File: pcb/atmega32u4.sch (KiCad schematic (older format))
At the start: 15 parts, among them CON1 ISP, P1 CONN_01X14, P2 CONN_01X14, P3 USB_OTG, U1 ATmega32U4-AU, Y1 16MHz

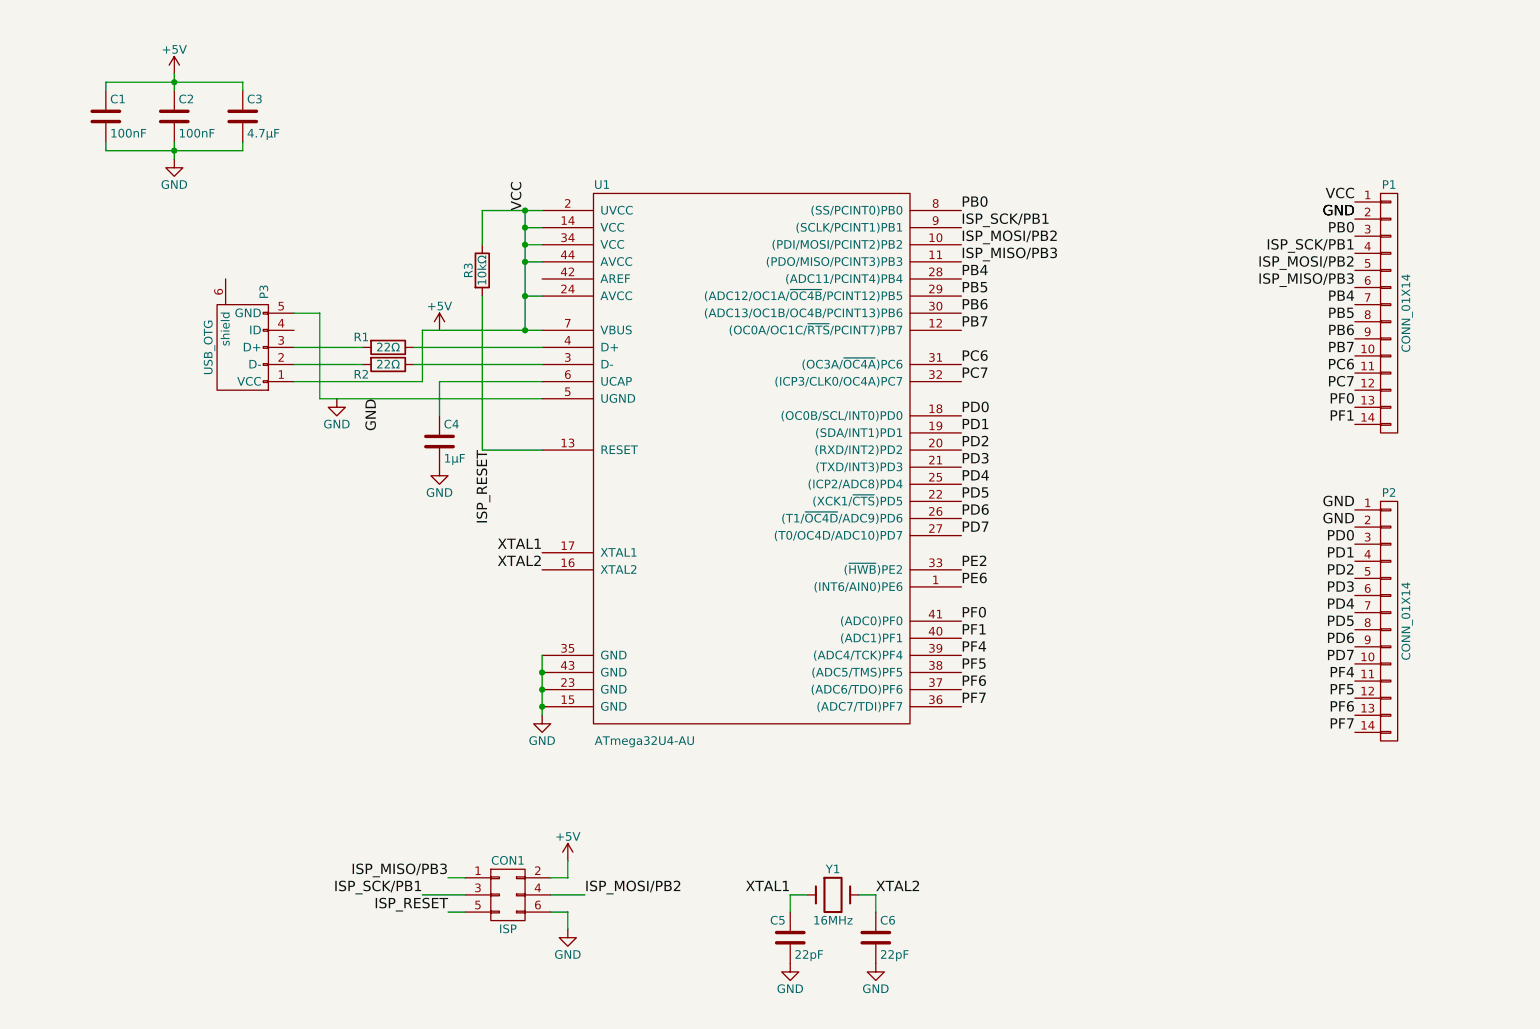
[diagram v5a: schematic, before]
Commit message: Fix up schematic accoring to adafruit
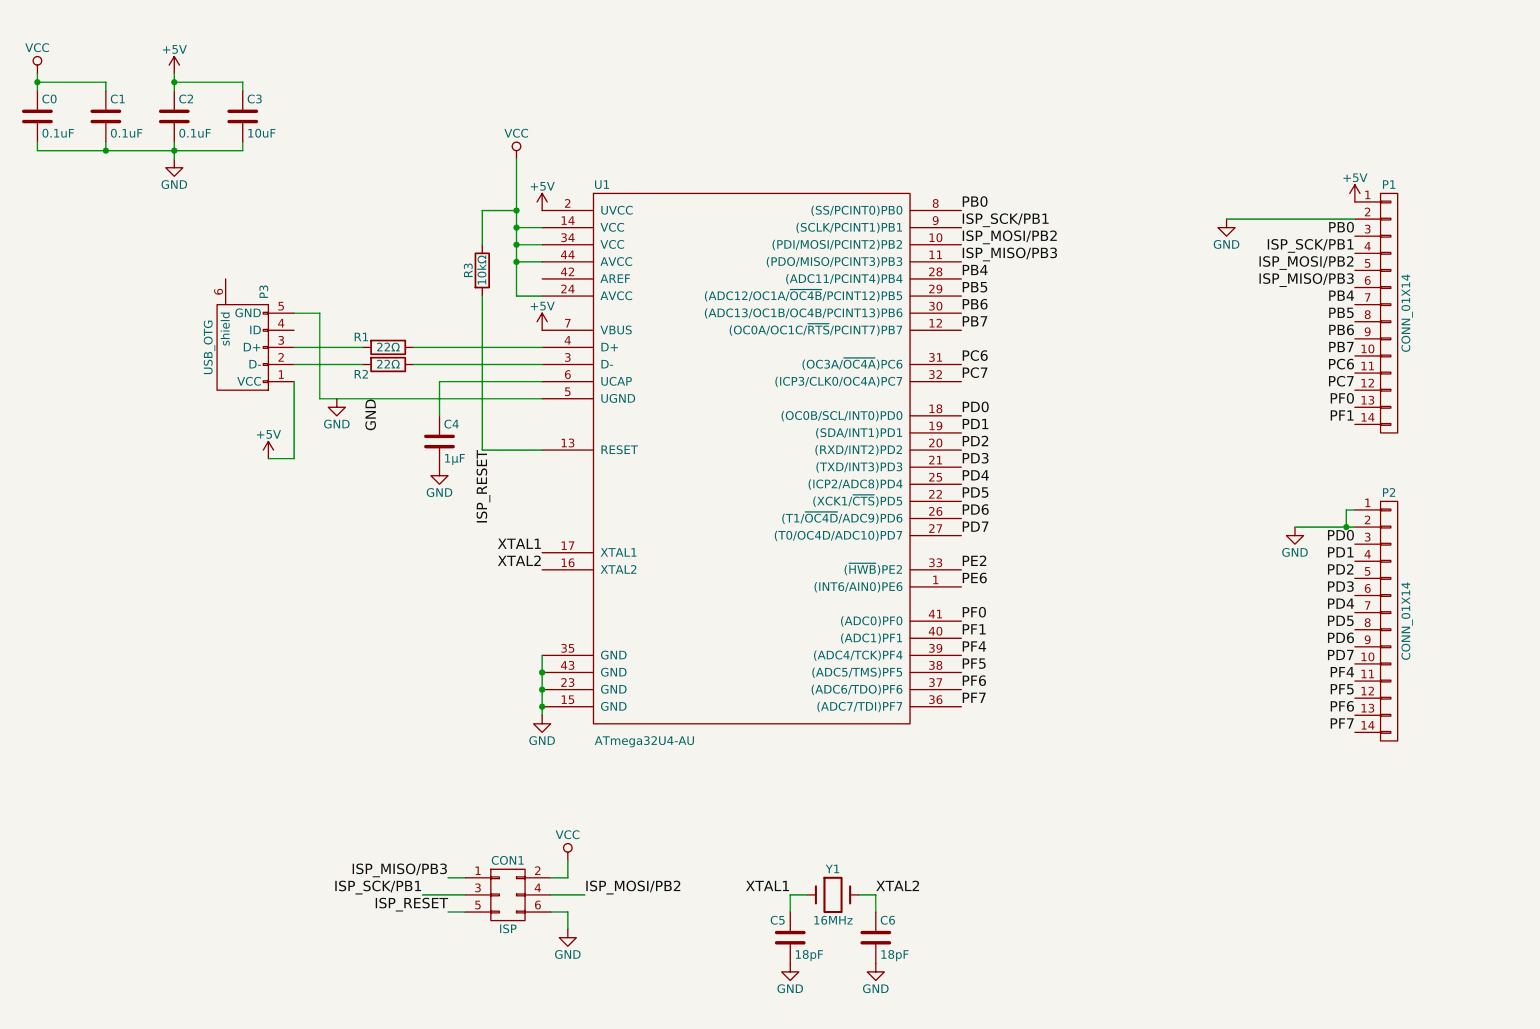
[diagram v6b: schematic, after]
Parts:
- added C0: 0.1uF, Capacitors_SMD:C_0805_HandSoldering, symbol C
- C1, C2: value 100nF -> 0.1uF
- C3: value 4.7µF -> 10uF
- C5, C6: value 22pF -> 18pF
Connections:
- net +5V: now also P1.1 (P1), P3.1 (VCC), U1.2 (UVCC), U1.7 (VBUS); no longer C1.1, CON1.2 (P2)
- net GND: now also C0.2
- net VCC: now also C1.1, CON1.2 (P2), C0.1; no longer P1.1 (P1), P3.1 (VCC), U1.2 (UVCC), U1.7 (VBUS)
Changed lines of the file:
@@
 P 1300 1350
 F 0 "C1" H 1325 1450 50  0000 L CNN
-F 1 "100nF" H 1325 1250 50  0000 L CNN
+F 1 "0.1uF" H 1325 1250 50  0000 L CNN
 F 2 "Capacitors_SMD:C_0805_HandSoldering" H 1338 1200 50  0001 C CNN
 F 3 "" H 1300 1350 50  0000 C CNN
@@
 P 1700 1350
 F 0 "C2" H 1725 1450 50  0000 L CNN
-F 1 "100nF" H 1725 1250 50  0000 L CNN
+F 1 "0.1uF" H 1725 1250 50  0000 L CNN
 F 2 "Capacitors_SMD:C_0805_HandSoldering" H 1738 1200 50  0001 C CNN
 F 3 "" H 1700 1350 50  0000 C CNN
@@
 P 2100 1350
 F 0 "C3" H 2125 1450 50  0000 L CNN
-F 1 "4.7µF" H 2125 1250 50  0000 L CNN
+F 1 "10uF" H 2125 1250 50  0000 L CNN
 F 2 "Capacitors_SMD:C_0805_HandSoldering" H 2138 1200 50  0001 C CNN
 F 3 "" H 2100 1350 50  0000 C CNN
@@
 	1    0    0    -1
 $EndComp
-Connection ~ 3750 2400
-Wire Wire Line
-	3500 1900 3850 1900
-Wire Wire Line
-	3500 3300 3500 2400
-Wire Wire Line
-	3850 3300 3500 3300
-Connection ~ 1700 1550
-Wire Wire Line
-	2100 1550 2100 1500
-Wire Wire Line
-	1300 1550 1300 1500
-Wire Wire Line
-	1300 1550 2100 1550
-Wire Wire Line
-	1700 1500 1700 1600
-Wire Wire Line
-	2100 1150 2100 1200
-Connection ~ 1700 1150
-Wire Wire Line
-	1300 1150 1300 1200
-Wire Wire Line
-	1300 1150 2100 1150
-Wire Wire Line
-	1700 1100 1700 1200
-Wire Wire Line
-	3850 4500 3850 4850
-Connection ~ 3850 4600
-Connection ~ 3850 4700
-Connection ~ 3850 4800
-Wire Wire Line
-	3850 2700 3100 2700
-Wire Wire Line
-	3100 2800 3850 2800
-Wire Wire Line
-	2800 2700 2400 2700
-Wire Wire Line
-	2400 2800 2800 2800
-Wire Wire Line
-	3150 2600 3850 2600
-Wire Wire Line
-	3150 2600 3150 2900
-Wire Wire Line
-	3150 2900 2400 2900
-Wire Wire Line
-	3750 2400 3850 2400
-Wire Wire Line
-	3750 1900 3750 2600
-Connection ~ 3750 2600
-Wire Wire Line
-	3850 3000 2550 3000
-Wire Wire Line
-	2550 3000 2550 2500
-Wire Wire Line
-	2550 2500 2400 2500
-Wire Wire Line
-	3850 2900 3250 2900
-Wire Wire Line
-	3250 2900 3250 3100
-Wire Wire Line
-	3500 1900 3500 2100
-Connection ~ 3750 1900
-Wire Wire Line
-	3850 2100 3750 2100
-Connection ~ 3750 2100
-Wire Wire Line
-	3750 2000 3850 2000
-Connection ~ 3750 2000
-Wire Wire Line
-	3850 2200 3750 2200
-Connection ~ 3750 2200
 Text Label 3550 3300 3    60   ~ 0
 ISP_RESET
@@
 Text Label 6300 2000 0    60   ~ 0
 ISP_SCK/PB1
-Wire Wire Line
-	3900 5800 4000 5800
-Wire Wire Line
-	4000 5800 4000 5700
-$Comp
-L +5V #PWR06
-U 1 1 57DFE2FD
-P 4000 5700
-F 0 "#PWR06" H 4000 5550 50  0001 C CNN
-F 1 "+5V" H 4000 5840 50  0000 C CNN
-F 2 "" H 4000 5700 50  0000 C CNN
-F 3 "" H 4000 5700 50  0000 C CNN
-	1    4000 5700
-	1    0    0    -1
-$EndComp
-Wire Wire Line
-	3900 6000 4000 6000
-Wire Wire Line
-	4000 6000 4000 6100
 $Comp
 L GND #PWR07
@@
 	1    0    0    -1
 $EndComp
-Wire Wire Line
-	3900 5900 4100 5900
 Text Label 4100 5900 0    60   ~ 0
 ISP_MOSI/PB2
-Wire Wire Line
-	3400 5900 3150 5900
 Text Label 3300 5800 2    60   ~ 0
 ISP_MISO/PB3
-Wire Wire Line
-	3400 5800 3300 5800
 Text Label 3150 5900 2    60   ~ 0
 ISP_SCK/PB1
-Wire Wire Line
-	3400 6000 3300 6000
 Text Label 3300 6000 2    60   ~ 0
 ISP_RESET
@@
 	1    0    0    -1
 $EndComp
-Wire Wire Line
-	5700 5900 5800 5900
-Wire Wire Line
-	5800 5900 5800 6000
-Wire Wire Line
-	5400 5900 5300 5900
-Wire Wire Line
-	5300 5900 5300 6000
 $Comp
 L C C6
@@
 P 5800 6150
 F 0 "C6" H 5825 6250 50  0000 L CNN
-F 1 "22pF" H 5825 6050 50  0000 L CNN
+F 1 "18pF" H 5825 6050 50  0000 L CNN
 F 2 "Capacitors_SMD:C_0805_HandSoldering" H 5838 6000 50  0001 C CNN
 F 3 "" H 5800 6150 50  0000 C CNN
@@
 P 5300 6150
 F 0 "C5" H 5182 6250 50  0000 L CNN
-F 1 "22pF" H 5325 6050 50  0000 L CNN
+F 1 "18pF" H 5325 6050 50  0000 L CNN
 F 2 "Capacitors_SMD:C_0805_HandSoldering" H 5338 6000 50  0001 C CNN
 F 3 "" H 5300 6150 50  0000 C CNN
@@
 	1    0    0    -1
 $EndComp
-Text Label 3750 1900 1    60   ~ 0
-VCC
 Text Label 2900 3000 3    60   ~ 0
-GND
-Text Label 8600 1850 2    60   ~ 0
-VCC
-Text Label 8600 1950 2    60   ~ 0
 GND
 Text Label 6300 1900 0    60   ~ 0
@@
 Text Label 8600 2950 2    60   ~ 0
 PC7
-Text Label 8600 1950 2    60   ~ 0
-GND
-Text Label 8600 3650 2    60   ~ 0
-GND
-Text Label 8600 3750 2    60   ~ 0
-GND
 Text Label 8600 3850 2    60   ~ 0
 PD0
@@
 L +5V #PWR010
 U 1 1 57E26C1F
-P 3250 2600
-F 0 "#PWR010" H 3250 2450 50  0001 C CNN
-F 1 "+5V" H 3250 2740 50  0000 C CNN
-F 2 "" H 3250 2600 50  0000 C CNN
-F 3 "" H 3250 2600 50  0000 C CNN
-	1    3250 2600
-	1    0    0    -1
-$EndComp
+P 3850 2600
+F 0 "#PWR010" H 3850 2450 50  0001 C CNN
+F 1 "+5V" H 3850 2740 50  0000 C CNN
+F 2 "" H 3850 2600 50  0000 C CNN
+F 3 "" H 3850 2600 50  0000 C CNN
+	1    3850 2600
+	1    0    0    -1
+$EndComp
+$Comp
+L +5V #PWR?
+U 1 1 57EB4CAF
+P 2250 3350
+F 0 "#PWR?" H 2250 3200 50  0001 C CNN
+F 1 "+5V" H 2250 3490 50  0000 C CNN
+F 2 "" H 2250 3350 50  0000 C CNN
+F 3 "" H 2250 3350 50  0000 C CNN
+	1    2250 3350
+	1    0    0    -1
+$EndComp
+$Comp
+L +5V #PWR?
+U 1 1 57EB53DC
+P 3850 1900
+F 0 "#PWR?" H 3850 1750 50  0001 C CNN
+F 1 "+5V" H 3850 2040 50  0000 C CNN
+F 2 "" H 3850 1900 50  0000 C CNN
+F 3 "" H 3850 1900 50  0000 C CNN
+	1    3850 1900
+	1    0    0    -1
+$EndComp
+$Comp
+L VCC #PWR?
+U 1 1 57EB59BD
+P 4000 5700
+F 0 "#PWR?" H 4000 5550 50  0001 C CNN
+F 1 "VCC" H 4000 5850 50  0000 C CNN
+F 2 "" H 4000 5700 50  0000 C CNN
+F 3 "" H 4000 5700 50  0000 C CNN
+	1    4000 5700
+	1    0    0    -1
+$EndComp
+$Comp
+L VCC #PWR?
+U 1 1 57EB5AB2
+P 3700 1600
+F 0 "#PWR?" H 3700 1450 50  0001 C CNN
+F 1 "VCC" H 3700 1750 50  0000 C CNN
+F 2 "" H 3700 1600 50  0000 C CNN
+F 3 "" H 3700 1600 50  0000 C CNN
+	1    3700 1600
+	1    0    0    -1
+$EndComp
+$Comp
+L +5V #PWR?
+U 1 1 57EB5C21
+P 8600 1850
+F 0 "#PWR?" H 8600 1700 50  0001 C CNN
+F 1 "+5V" H 8600 1990 50  0000 C CNN
+F 2 "" H 8600 1850 50  0000 C CNN
+F 3 "" H 8600 1850 50  0000 C CNN
+	1    8600 1850
+	1    0    0    -1
+$EndComp
+$Comp
+L GND #PWR?
+U 1 1 57EB5F9C
+P 8250 3750
+F 0 "#PWR?" H 8250 3500 50  0001 C CNN
+F 1 "GND" H 8250 3600 50  0000 C CNN
+F 2 "" H 8250 3750 50  0000 C CNN
+F 3 "" H 8250 3750 50  0000 C CNN
+	1    8250 3750
+	1    0    0    -1
+$EndComp
+Wire Wire Line
+	3500 3300 3500 2400
+Wire Wire Line
+	3850 3300 3500 3300
+Connection ~ 1700 1550
+Wire Wire Line
+	2100 1550 2100 1500
+Wire Wire Line
+	1300 1550 1300 1500
+Wire Wire Line
+	900  1550 2100 1550
+Wire Wire Line
+	1700 1500 1700 1600
+Wire Wire Line
+	3850 4500 3850 4850
+Connection ~ 3850 4600
+Connection ~ 3850 4700
+Connection ~ 3850 4800
+Wire Wire Line
+	3850 2700 3100 2700
+Wire Wire Line
+	3100 2800 3850 2800
+Wire Wire Line
+	2800 2700 2400 2700
+Wire Wire Line
+	2400 2800 2800 2800
+Wire Wire Line
+	3850 3000 2550 3000
+Wire Wire Line
+	2550 3000 2550 2500
+Wire Wire Line
+	2550 2500 2400 2500
+Wire Wire Line
+	3850 2900 3250 2900
+Wire Wire Line
+	3250 2900 3250 3100
+Wire Wire Line
+	3900 5800 4000 5800
+Wire Wire Line
+	4000 5800 4000 5700
+Wire Wire Line
+	3900 6000 4000 6000
+Wire Wire Line
+	4000 6000 4000 6100
+Wire Wire Line
+	3900 5900 4100 5900
+Wire Wire Line
+	3400 5900 3150 5900
+Wire Wire Line
+	3400 5800 3300 5800
+Wire Wire Line
+	3400 6000 3300 6000
+Wire Wire Line
+	5700 5900 5800 5900
+Wire Wire Line
+	5800 5900 5800 6000
+Wire Wire Line
+	5400 5900 5300 5900
+Wire Wire Line
+	5300 5900 5300 6000
+Wire Wire Line
+	2400 2900 2400 3350
+Wire Wire Line
+	2400 3350 2250 3350
+Wire Wire Line
+	3850 2400 3700 2400
+Wire Wire Line
+	3700 2400 3700 1600
+Wire Wire Line
+	3850 2200 3700 2200
+Connection ~ 3700 2200
+Wire Wire Line
+	3850 2100 3700 2100
+Connection ~ 3700 2100
+Wire Wire Line
+	3850 2000 3700 2000
+Connection ~ 3700 2000
+Wire Wire Line
+	8250 3750 8600 3750
+Wire Wire Line
+	8600 3650 8550 3650
+Wire Wire Line
+	8550 3650 8550 3750
+Connection ~ 8550 3750
+Wire Wire Line
+	7850 1950 8600 1950
+$Comp
+L GND #PWR?
+U 1 1 57EB672F
+P 7850 1950
+F 0 "#PWR?" H 7850 1700 50  0001 C CNN
+F 1 "GND" H 7850 1800 50  0000 C CNN
+F 2 "" H 7850 1950 50  0000 C CNN
+F 3 "" H 7850 1950 50  0000 C CNN
+	1    7850 1950
+	1    0    0    -1
+$EndComp
+$Comp
+L C C0
+U 1 1 57EBA764
+P 900 1350
+F 0 "C0" H 925 1450 50  0000 L CNN
+F 1 "0.1uF" H 925 1250 50  0000 L CNN
+F 2 "Capacitors_SMD:C_0805_HandSoldering" H 938 1200 50  0001 C CNN
+F 3 "" H 900 1350 50  0000 C CNN
+	1    900  1350
+	1    0    0    -1
+$EndComp
+$Comp
+L VCC #PWR?
+U 1 1 57EBA95D
+P 900 1100
+F 0 "#PWR?" H 900 950 50  0001 C CNN
+F 1 "VCC" H 900 1250 50  0000 C CNN
+F 2 "" H 900 1100 50  0000 C CNN
+F 3 "" H 900 1100 50  0000 C CNN
+	1    900  1100
+	1    0    0    -1
+$EndComp
+Wire Wire Line
+	900  1100 900  1200
+Wire Wire Line
+	900  1150 1300 1150
+Wire Wire Line
+	1300 1150 1300 1200
+Connection ~ 900  1150
+Wire Wire Line
+	1700 1100 1700 1200
+Wire Wire Line
+	1700 1150 2100 1150
+Wire Wire Line
+	2100 1150 2100 1200
+Connection ~ 1700 1150
+Wire Wire Line
+	900  1500 900  1550
+Connection ~ 1300 1550
+Wire Wire Line
+	3500 2100 3500 1900
+Wire Wire Line
+	3500 1900 3700 1900
+Connection ~ 3700 1900
 $EndSCHEMATC

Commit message: Rearrange pins
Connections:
- net GND: no longer P2.2 (P2)
- net ISP_MISO/PB3: now also P2.10 (P10); no longer P1.6 (P6)
- net ISP_MOSI/PB2: now also P2.11 (P11); no longer P1.5 (P5)
- net ISP_SCK/PB1: now also P2.12 (P12); no longer P1.4 (P4)
- net PB0: now also P2.13 (P13); no longer P1.3 (P3)
- net PB4: now also P1.14 (P14); no longer P1.7 (P7)
- net PB5: now also P1.13 (P13); no longer P1.8 (P8)
- net PB6: now also P1.12 (P12); no longer P1.9 (P9)
- net PB7: now also P1.11 (P11); no longer P1.10 (P10)
- net PC6: now also P1.10 (P10); no longer P1.11 (P11)
- net PC7: now also P1.9 (P9); no longer P1.12 (P12)
- net PD0: now also P2.9 (P9); no longer P2.3 (P3)
- net PD1: now also P2.8 (P8); no longer P2.4 (P4)
- net PD2: now also P2.7 (P7); no longer P2.5 (P5)
- net PD4: now also P2.5 (P5); no longer P2.7 (P7)
- net PD5: now also P2.4 (P4); no longer P2.8 (P8)
- net PD6: now also P2.3 (P3); no longer P2.9 (P9)
- net PD7: now also P2.2 (P2); no longer P2.10 (P10)
- net PF0: now also P1.3 (P3); no longer P1.13 (P13)
- net PF1: now also P1.4 (P4); no longer P1.14 (P14)
- net PF4: now also P1.5 (P5); no longer P2.11 (P11)
- net PF5: now also P1.6 (P6); no longer P2.12 (P12)
- net PF6: now also P1.7 (P7); no longer P2.13 (P13)
- net PF7: now also P1.8 (P8); no longer P2.14 (P14)
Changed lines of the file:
@@
 Text Label 6300 4800 0    60   ~ 0
 PF7
-Text Label 8600 2250 2    60   ~ 0
+Text Label 8600 4650 2    60   ~ 0
 ISP_MOSI/PB2
-Text Label 8600 2350 2    60   ~ 0
+Text Label 8600 4550 2    60   ~ 0
 ISP_MISO/PB3
-Text Label 8600 2150 2    60   ~ 0
+Text Label 8600 4750 2    60   ~ 0
 ISP_SCK/PB1
-Text Label 8600 2050 2    60   ~ 0
+Text Label 8600 4850 2    60   ~ 0
 PB0
-Text Label 8600 2450 2    60   ~ 0
+Text Label 8600 3150 2    60   ~ 0
 PB4
-Text Label 8600 2550 2    60   ~ 0
+Text Label 8600 3050 2    60   ~ 0
 PB5
+Text Label 8600 2950 2    60   ~ 0
+PB6
+Text Label 8600 2850 2    60   ~ 0
+PB7
+Text Label 8600 2750 2    60   ~ 0
+PC6
 Text Label 8600 2650 2    60   ~ 0
-PB6
-Text Label 8600 2750 2    60   ~ 0
-PB7
-Text Label 8600 2850 2    60   ~ 0
-PC6
-Text Label 8600 2950 2    60   ~ 0
 PC7
-Text Label 8600 3850 2    60   ~ 0
+Text Label 8600 4450 2    60   ~ 0
 PD0
-Text Label 8600 3950 2    60   ~ 0
+Text Label 8600 4350 2    60   ~ 0
 PD1
-Text Label 8600 4050 2    60   ~ 0
+Text Label 8600 4250 2    60   ~ 0
 PD2
 Text Label 8600 4150 2    60   ~ 0
 PD3
-Text Label 8600 4250 2    60   ~ 0
+Text Label 8600 4050 2    60   ~ 0
 PD4
-Text Label 8600 4350 2    60   ~ 0
+Text Label 8600 3950 2    60   ~ 0
 PD5
-Text Label 8600 4450 2    60   ~ 0
+Text Label 8600 3850 2    60   ~ 0
 PD6
-Text Label 8600 4550 2    60   ~ 0
+Text Label 8600 3750 2    60   ~ 0
 PD7
 $Comp
@@
 	1    0    0    -1
 $EndComp
-Text Label 8600 3050 2    60   ~ 0
+Text Label 8600 2050 2    60   ~ 0
 PF0
-Text Label 8600 3150 2    60   ~ 0
+Text Label 8600 2150 2    60   ~ 0
 PF1
-Text Label 8600 4650 2    60   ~ 0
+Text Label 8600 2250 2    60   ~ 0
 PF4
-Text Label 8600 4750 2    60   ~ 0
+Text Label 8600 2350 2    60   ~ 0
 PF5
-Text Label 8600 4850 2    60   ~ 0
+Text Label 8600 2450 2    60   ~ 0
 PF6
-Text Label 8600 4950 2    60   ~ 0
+Text Label 8600 2550 2    60   ~ 0
 PF7
 $Comp
@@
 L GND #PWR?
 U 1 1 57EB5F9C
-P 8250 3750
-F 0 "#PWR?" H 8250 3500 50  0001 C CNN
-F 1 "GND" H 8250 3600 50  0000 C CNN
-F 2 "" H 8250 3750 50  0000 C CNN
-F 3 "" H 8250 3750 50  0000 C CNN
-	1    8250 3750
+P 8250 3650
+F 0 "#PWR?" H 8250 3400 50  0001 C CNN
+F 1 "GND" H 8250 3500 50  0000 C CNN
+F 2 "" H 8250 3650 50  0000 C CNN
+F 3 "" H 8250 3650 50  0000 C CNN
+	1    8250 3650
 	1    0    0    -1
 $EndComp
@@
 	3850 2000 3700 2000
 Connection ~ 3700 2000
-Wire Wire Line
-	8250 3750 8600 3750
-Wire Wire Line
-	8600 3650 8550 3650
-Wire Wire Line
-	8550 3650 8550 3750
-Connection ~ 8550 3750
 Wire Wire Line
 	7850 1950 8600 1950
@@
 	3500 1900 3700 1900
 Connection ~ 3700 1900
+Wire Wire Line
+	8600 3650 8250 3650
 $EndSCHEMATC

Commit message: Add LEDs
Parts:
- added D1: RED, symbol LED
- added D2: GREED, symbol LED
- added R4, R5: 1K, symbol R
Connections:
- net +5V: now also R5.1
- net GND: now also D1.1 (K), D2.1 (K)
- net PE6: now also P2.14 (P14), R4.1
- new net: D1.2 (A), R4.2
- new net: D2.2 (A), R5.2
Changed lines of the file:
@@
 Wire Wire Line
 	8600 3650 8250 3650
+$Comp
+L R R4
+U 1 1 57EBBD06
+P 8600 5100
+F 0 "R4" V 8680 5100 50  0000 C CNN
+F 1 "1K" V 8600 5100 50  0000 C CNN
+F 2 "" V 8530 5100 50  0000 C CNN
+F 3 "" H 8600 5100 50  0000 C CNN
+	1    8600 5100
+	1    0    0    -1
+$EndComp
+$Comp
+L LED D1
+U 1 1 57EBBDD1
+P 8600 5450
+F 0 "D1" H 8600 5550 50  0000 C CNN
+F 1 "RED" H 8600 5350 50  0000 C CNN
+F 2 "" H 8600 5450 50  0000 C CNN
+F 3 "" H 8600 5450 50  0000 C CNN
+	1    8600 5450
+	0    -1   -1   0
+$EndComp
+$Comp
+L GND #PWR?
+U 1 1 57EBBE20
+P 8600 5650
+F 0 "#PWR?" H 8600 5400 50  0001 C CNN
+F 1 "GND" H 8600 5500 50  0000 C CNN
+F 2 "" H 8600 5650 50  0000 C CNN
+F 3 "" H 8600 5650 50  0000 C CNN
+	1    8600 5650
+	1    0    0    -1
+$EndComp
+$Comp
+L R R5
+U 1 1 57EBBF78
+P 9450 5100
+F 0 "R5" V 9530 5100 50  0000 C CNN
+F 1 "1K" V 9450 5100 50  0000 C CNN
+F 2 "" V 9380 5100 50  0000 C CNN
+F 3 "" H 9450 5100 50  0000 C CNN
+	1    9450 5100
+	1    0    0    -1
+$EndComp
+$Comp
+L LED D2
+U 1 1 57EBBF7E
+P 9450 5450
+F 0 "D2" H 9450 5550 50  0000 C CNN
+F 1 "GREED" H 9450 5350 50  0000 C CNN
+F 2 "" H 9450 5450 50  0000 C CNN
+F 3 "" H 9450 5450 50  0000 C CNN
+	1    9450 5450
+	0    -1   -1   0
+$EndComp
+$Comp
+L GND #PWR?
+U 1 1 57EBBF84
+P 9450 5650
+F 0 "#PWR?" H 9450 5400 50  0001 C CNN
+F 1 "GND" H 9450 5500 50  0000 C CNN
+F 2 "" H 9450 5650 50  0000 C CNN
+F 3 "" H 9450 5650 50  0000 C CNN
+	1    9450 5650
+	1    0    0    -1
+$EndComp
+$Comp
+L +5V #PWR?
+U 1 1 57EBBFA2
+P 9450 4950
+F 0 "#PWR?" H 9450 4800 50  0001 C CNN
+F 1 "+5V" H 9450 5090 50  0000 C CNN
+F 2 "" H 9450 4950 50  0000 C CNN
+F 3 "" H 9450 4950 50  0000 C CNN
+	1    9450 4950
+	1    0    0    -1
+$EndComp
+Text Label 8600 4950 2    60   ~ 0
+PE6
 $EndSCHEMATC
